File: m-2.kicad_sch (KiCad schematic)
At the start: 14 parts, among them Y2 Oscillator_SMD_32.768kHz_ECS_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

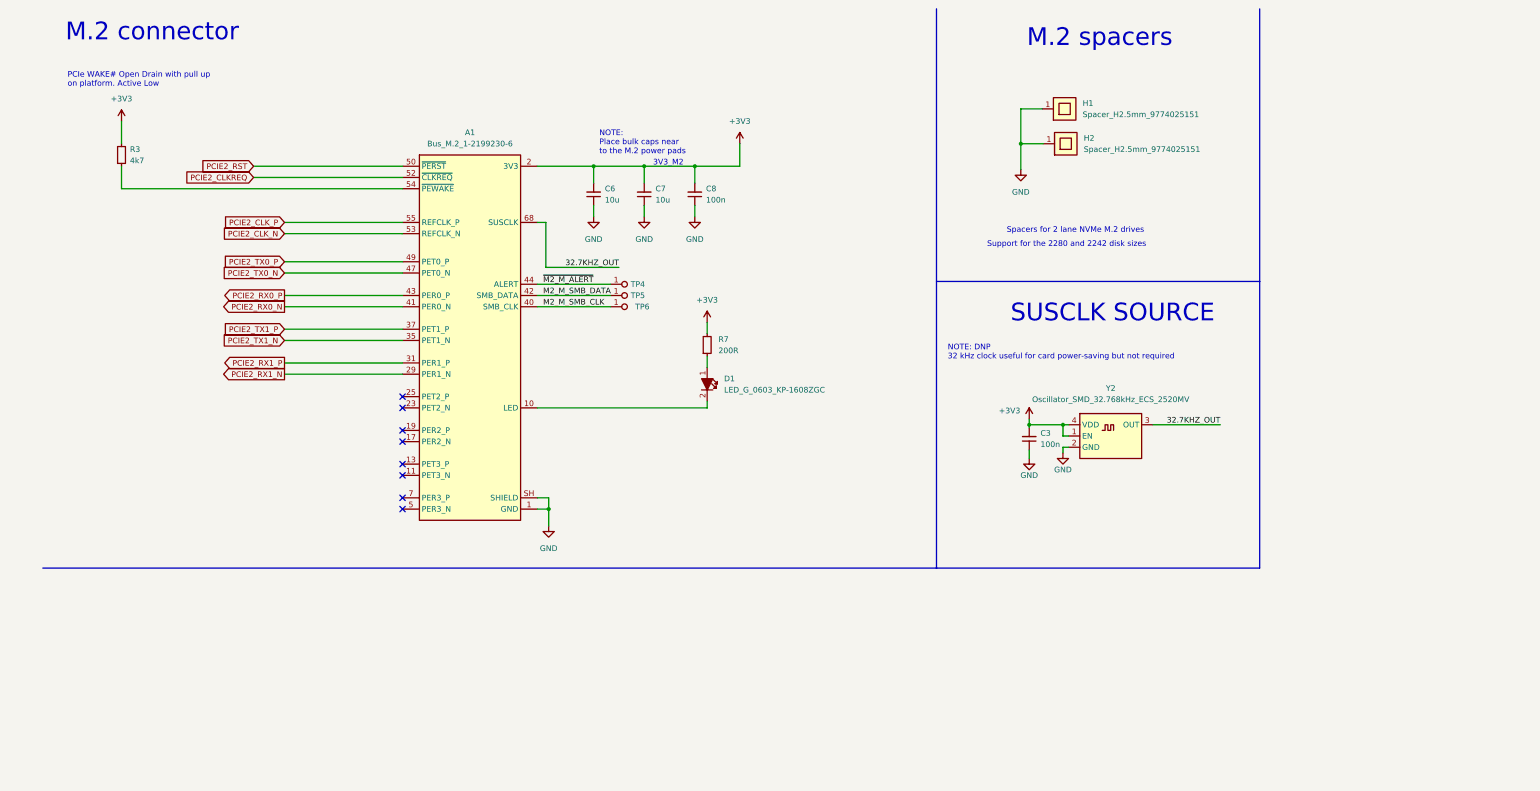
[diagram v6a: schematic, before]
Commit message: [#45990] Fix silk screen drcs
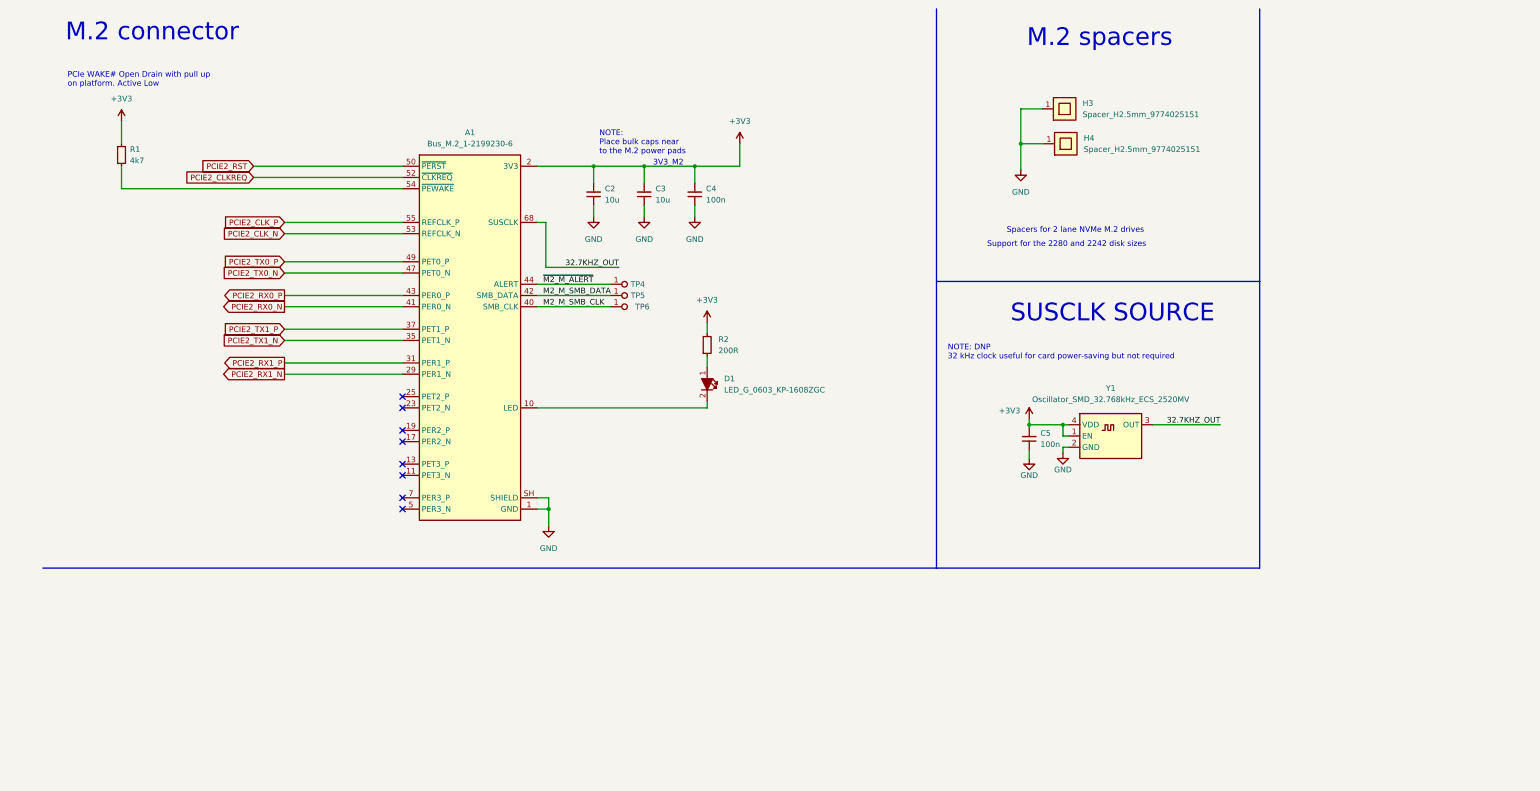
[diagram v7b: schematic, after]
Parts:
- renumbered C6 to C2, C7 to C3, C8 to C4, C3 to C5, H1 to H3, H2 to H4, R3 to R1, R7 to R2, Y2 to Y1
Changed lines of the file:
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@@
   (symbol (lib_id "antmicropower:GND") (at 136.525 59.055 0) (unit 1)
     (in_bom yes) (on_board yes) (fields_autoplaced)
-    (property "Reference" "#PWR011" (id 0) (at 136.525 65.405 0)
+    (property "Reference" "#PWR08" (id 0) (at 136.525 65.405 0)
       (effects (font (size 1.27 1.27)) hide)
     )
@@
   (symbol (lib_id "jetson-orin-baseboard:GND") (at 234.95 113.665 0) (mirror y) (unit 1)
     (in_bom yes) (on_board yes) (fields_autoplaced)
-    (property "Reference" "#PWR0106" (id 0) (at 234.95 120.015 0)
+    (property "Reference" "#PWR015" (id 0) (at 234.95 120.015 0)
       (effects (font (size 1.27 1.27)) hide)
     )
@@
   (symbol (lib_id "antmicropower:+3V3") (at 169.545 42.545 0) (unit 1)
     (in_bom yes) (on_board yes) (fields_autoplaced)
-    (property "Reference" "#PWR015" (id 0) (at 169.545 46.355 0)
+    (property "Reference" "#PWR012" (id 0) (at 169.545 46.355 0)
       (effects (font (size 1.27 1.27)) hide)
     )
@@
   (symbol (lib_id "antmicroMechanicalParts:Spacer_H2.5mm_9774025151") (at 237.871 34.671 0) (unit 1)
     (in_bom yes) (on_board yes) (fields_autoplaced)
-    (property "Reference" "H1" (id 0) (at 247.015 33.4009 0)
+    (property "Reference" "H3" (id 0) (at 247.015 33.4009 0)
       (effects (font (size 1.27 1.27) (thickness 0.15)) (justify left))
     )
@@
   (symbol (lib_id "antmicropower:GND") (at 159.385 59.055 0) (unit 1)
     (in_bom yes) (on_board yes) (fields_autoplaced)
-    (property "Reference" "#PWR014" (id 0) (at 159.385 65.405 0)
+    (property "Reference" "#PWR010" (id 0) (at 159.385 65.405 0)
       (effects (font (size 1.27 1.27)) hide)
     )
@@
   (symbol (lib_id "antmicroCapacitors0402:C_100n_0402") (at 234.95 111.76 90) (unit 1)
     (in_bom yes) (on_board yes) (fields_autoplaced)
-    (property "Reference" "C3" (id 0) (at 237.49 107.9435 90)
+    (property "Reference" "C5" (id 0) (at 237.49 107.9435 90)
       (effects (font (size 1.27 1.27) (thickness 0.15)) (justify right))
     )
@@
   (symbol (lib_id "antmicroResistors0402:R_200R_0402") (at 162.179 90.551 90) (unit 1)
     (in_bom yes) (on_board yes) (fields_autoplaced)
-    (property "Reference" "R7" (id 0) (at 164.719 86.7409 90)
+    (property "Reference" "R2" (id 0) (at 164.719 86.7409 90)
       (effects (font (size 1.27 1.27) (thickness 0.15)) (justify right))
     )
@@
   (symbol (lib_id "antmicroOscillators:Oscillator_SMD_32.768kHz_ECS_2520MV") (at 243.84 106.045 0) (unit 1)
     (in_bom yes) (on_board yes) (fields_autoplaced)
-    (property "Reference" "Y2" (id 0) (at 253.365 97.79 0)
+    (property "Reference" "Y1" (id 0) (at 253.365 97.79 0)
       (effects (font (size 1.27 1.27) (thickness 0.15)))
     )
@@
   (symbol (lib_id "antmicroCapacitors0402:C_10u_0402") (at 147.955 56.515 90) (unit 1)
     (in_bom yes) (on_board yes) (fields_autoplaced)
-    (property "Reference" "C7" (id 0) (at 150.495 52.6985 90)
+    (property "Reference" "C3" (id 0) (at 150.495 52.6985 90)
       (effects (font (size 1.27 1.27) (thickness 0.15)) (justify right))
     )
@@
   (symbol (lib_id "antmicropower:GND") (at 233.045 48.387 0) (unit 1)
     (in_bom yes) (on_board yes) (fields_autoplaced)
-    (property "Reference" "#PWR0101" (id 0) (at 233.045 54.737 0)
+    (property "Reference" "#PWR013" (id 0) (at 233.045 54.737 0)
       (effects (font (size 1.27 1.27)) hide)
     )
@@
   (symbol (lib_id "antmicropower:+3V3") (at 162.179 82.931 0) (unit 1)
     (in_bom yes) (on_board yes) (fields_autoplaced)
-    (property "Reference" "#PWR012" (id 0) (at 162.179 86.741 0)
+    (property "Reference" "#PWR011" (id 0) (at 162.179 86.741 0)
       (effects (font (size 1.27 1.27)) hide)
     )
@@
   (symbol (lib_id "antmicroResistors0402:R_4k7_0402") (at 29.845 47.625 90) (unit 1)
     (in_bom yes) (on_board yes) (fields_autoplaced)
-    (property "Reference" "R3" (id 0) (at 31.75 43.8149 90)
+    (property "Reference" "R1" (id 0) (at 31.75 43.8149 90)
       (effects (font (size 1.27 1.27) (thickness 0.15)) (justify right))
     )
@@
   (symbol (lib_id "antmicroMechanicalParts:Spacer_H2.5mm_9774025151") (at 238.125 42.545 0) (unit 1)
     (in_bom yes) (on_board yes) (fields_autoplaced)
-    (property "Reference" "H2" (id 0) (at 247.269 41.2749 0)
+    (property "Reference" "H4" (id 0) (at 247.269 41.2749 0)
       (effects (font (size 1.27 1.27) (thickness 0.15)) (justify left))
     )
@@
   (symbol (lib_id "antmicroCapacitors0603:C_100n_0603") (at 159.385 56.515 90) (unit 1)
     (in_bom yes) (on_board yes) (fields_autoplaced)
-    (property "Reference" "C8" (id 0) (at 161.925 52.6985 90)
+    (property "Reference" "C4" (id 0) (at 161.925 52.6985 90)
       (effects (font (size 1.27 1.27) (thickness 0.15)) (justify right))
     )
@@
   (symbol (lib_id "jetson-orin-baseboard:+3V3") (at 234.95 104.775 0) (unit 1)
     (in_bom yes) (on_board yes)
-    (property "Reference" "#PWR0107" (id 0) (at 234.95 108.585 0)
+    (property "Reference" "#PWR014" (id 0) (at 234.95 108.585 0)
       (effects (font (size 1.27 1.27)) hide)
     )
@@
   (symbol (lib_id "antmicroCapacitors0402:C_10u_0402") (at 136.525 56.515 90) (unit 1)
     (in_bom yes) (on_board yes) (fields_autoplaced)
-    (property "Reference" "C6" (id 0) (at 139.065 52.6985 90)
+    (property "Reference" "C2" (id 0) (at 139.065 52.6985 90)
       (effects (font (size 1.27 1.27) (thickness 0.15)) (justify right))
     )
@@
   (symbol (lib_id "jetson-orin-baseboard:GND") (at 242.57 112.395 0) (unit 1)
     (in_bom yes) (on_board yes) (fields_autoplaced)
-    (property "Reference" "#PWR0104" (id 0) (at 242.57 118.745 0)
+    (property "Reference" "#PWR016" (id 0) (at 242.57 118.745 0)
       (effects (font (size 1.27 1.27)) hide)
     )
@@
   (symbol (lib_id "antmicropower:+3V3") (at 29.845 37.465 0) (unit 1)
     (in_bom yes) (on_board yes) (fields_autoplaced)
-    (property "Reference" "#PWR09" (id 0) (at 29.845 41.275 0)
+    (property "Reference" "#PWR06" (id 0) (at 29.845 41.275 0)
       (effects (font (size 1.27 1.27)) hide)
     )
@@
   (symbol (lib_id "antmicropower:GND") (at 126.365 128.905 0) (unit 1)
     (in_bom yes) (on_board yes) (fields_autoplaced)
-    (property "Reference" "#PWR010" (id 0) (at 126.365 135.255 0)
+    (property "Reference" "#PWR07" (id 0) (at 126.365 135.255 0)
       (effects (font (size 1.27 1.27)) hide)
     )
@@
   (symbol (lib_id "antmicropower:GND") (at 147.955 59.055 0) (unit 1)
     (in_bom yes) (on_board yes) (fields_autoplaced)
-    (property "Reference" "#PWR013" (id 0) (at 147.955 65.405 0)
-      (effects (font (size 1.27 1.27)) hide)
-    )
+    (property "Reference" "#PWR09" (id 0) (at 147.955 65.405 0)
+      (effects (font (size 1.27 1.27)) hide)
+    )

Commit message: [#45990] Cosmetic changes for schematic, expand README
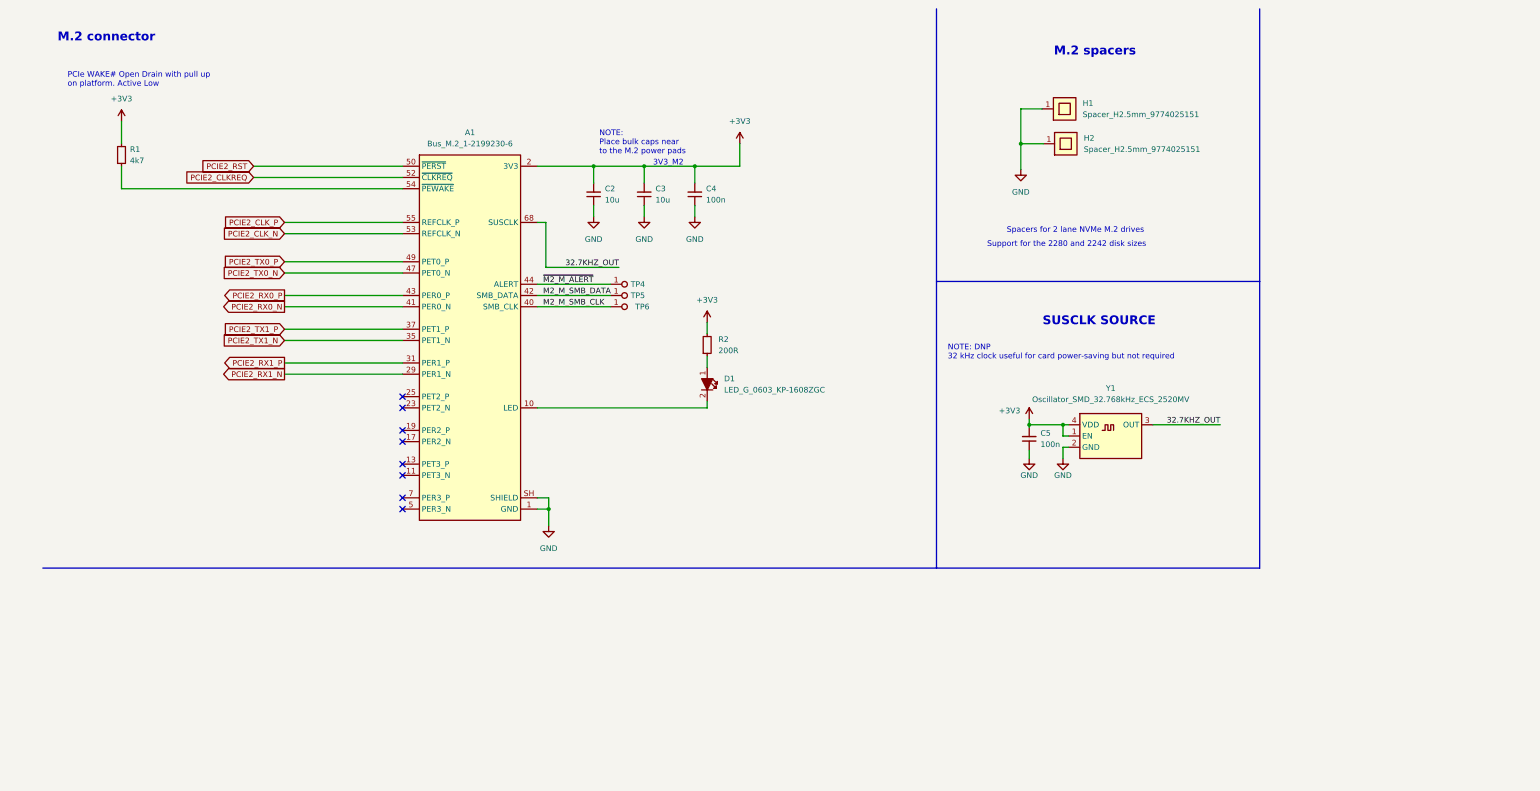
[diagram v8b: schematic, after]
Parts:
- renumbered H3 to H1, H4 to H2
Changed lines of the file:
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@@
     (stroke (width 0) (type default) (color 0 0 0 0))
   )
-  (wire (pts (xy 242.57 111.125) (xy 242.57 112.395))
+  (wire (pts (xy 242.57 111.125) (xy 242.57 113.665))
     (stroke (width 0) (type default) (color 0 0 0 0))
   )
@@
     (effects (font (size 1.27 1.27)) (justify left bottom))
   )
-  (text "M.2 spacers" (at 267.335 20.955 180)
-    (effects (font (size 4 4)) (justify right bottom))
-  )
-  (text "M.2 connector" (at 56.388 19.685 180)
-    (effects (font (size 4 4)) (justify right bottom))
+  (text "M.2 spacers" (at 259.08 22.86 180)
+    (effects (font (size 2 2) (thickness 0.4) bold) (justify right bottom))
+  )
+  (text "M.2 connector" (at 37.465 19.685 180)
+    (effects (font (size 2 2) (thickness 0.4) bold) (justify right bottom))
   )
   (text "Spacers for 2 lane NVMe M.2 drives" (at 229.87 62.865 0)
     (effects (font (size 1.27 1.27)) (justify left bottom))
   )
-  (text "SUSCLK SOURCE" (at 276.86 83.185 180)
-    (effects (font (size 4 4)) (justify right bottom))
+  (text "SUSCLK SOURCE" (at 263.525 83.82 180)
+    (effects (font (size 2 2) (thickness 0.4) bold) (justify right bottom))
   )
   (text "NOTE:\nPlace bulk caps near \nto the M.2 power pads" (at 137.795 45.085 0)
@@
   (symbol (lib_id "antmicropower:GND") (at 136.525 59.055 0) (unit 1)
     (in_bom yes) (on_board yes) (fields_autoplaced)
-    (property "Reference" "#PWR08" (id 0) (at 136.525 65.405 0)
+    (property "Reference" "#PWR07" (id 0) (at 136.525 65.405 0)
       (effects (font (size 1.27 1.27)) hide)
     )
@@
   (symbol (lib_id "jetson-orin-baseboard:GND") (at 234.95 113.665 0) (mirror y) (unit 1)
     (in_bom yes) (on_board yes) (fields_autoplaced)
-    (property "Reference" "#PWR015" (id 0) (at 234.95 120.015 0)
+    (property "Reference" "#PWR014" (id 0) (at 234.95 120.015 0)
       (effects (font (size 1.27 1.27)) hide)
     )
@@
   (symbol (lib_id "antmicropower:+3V3") (at 169.545 42.545 0) (unit 1)
     (in_bom yes) (on_board yes) (fields_autoplaced)
-    (property "Reference" "#PWR012" (id 0) (at 169.545 46.355 0)
+    (property "Reference" "#PWR011" (id 0) (at 169.545 46.355 0)
       (effects (font (size 1.27 1.27)) hide)
     )
@@
   (symbol (lib_id "antmicroMechanicalParts:Spacer_H2.5mm_9774025151") (at 237.871 34.671 0) (unit 1)
     (in_bom yes) (on_board yes) (fields_autoplaced)
-    (property "Reference" "H3" (id 0) (at 247.015 33.4009 0)
+    (property "Reference" "H1" (id 0) (at 247.015 33.4009 0)
       (effects (font (size 1.27 1.27) (thickness 0.15)) (justify left))
     )
@@
   (symbol (lib_id "antmicropower:GND") (at 159.385 59.055 0) (unit 1)
     (in_bom yes) (on_board yes) (fields_autoplaced)
-    (property "Reference" "#PWR010" (id 0) (at 159.385 65.405 0)
+    (property "Reference" "#PWR09" (id 0) (at 159.385 65.405 0)
       (effects (font (size 1.27 1.27)) hide)
     )
@@
   (symbol (lib_id "antmicropower:GND") (at 233.045 48.387 0) (unit 1)
     (in_bom yes) (on_board yes) (fields_autoplaced)
-    (property "Reference" "#PWR013" (id 0) (at 233.045 54.737 0)
+    (property "Reference" "#PWR012" (id 0) (at 233.045 54.737 0)
       (effects (font (size 1.27 1.27)) hide)
     )
@@
   (symbol (lib_id "antmicropower:+3V3") (at 162.179 82.931 0) (unit 1)
     (in_bom yes) (on_board yes) (fields_autoplaced)
-    (property "Reference" "#PWR011" (id 0) (at 162.179 86.741 0)
+    (property "Reference" "#PWR010" (id 0) (at 162.179 86.741 0)
       (effects (font (size 1.27 1.27)) hide)
     )
@@
   (symbol (lib_id "antmicroMechanicalParts:Spacer_H2.5mm_9774025151") (at 238.125 42.545 0) (unit 1)
     (in_bom yes) (on_board yes) (fields_autoplaced)
-    (property "Reference" "H4" (id 0) (at 247.269 41.2749 0)
+    (property "Reference" "H2" (id 0) (at 247.269 41.2749 0)
       (effects (font (size 1.27 1.27) (thickness 0.15)) (justify left))
     )
@@
   (symbol (lib_id "jetson-orin-baseboard:+3V3") (at 234.95 104.775 0) (unit 1)
     (in_bom yes) (on_board yes)
-    (property "Reference" "#PWR014" (id 0) (at 234.95 108.585 0)
+    (property "Reference" "#PWR013" (id 0) (at 234.95 108.585 0)
       (effects (font (size 1.27 1.27)) hide)
     )
@@
     (pin "2")
   )
-  (symbol (lib_id "jetson-orin-baseboard:GND") (at 242.57 112.395 0) (unit 1)
+  (symbol (lib_id "jetson-orin-baseboard:GND") (at 242.57 113.665 0) (unit 1)
     (in_bom yes) (on_board yes) (fields_autoplaced)
-    (property "Reference" "#PWR016" (id 0) (at 242.57 118.745 0)
-      (effects (font (size 1.27 1.27)) hide)
-    )
-    (property "Value" "GND" (id 1) (at 242.57 116.205 0))
-    (property "Footprint" "" (id 2) (at 242.57 112.395 0)
-      (effects (font (size 1.27 1.27)) hide)
-    )
-    (property "Datasheet" "" (id 3) (at 242.57 112.395 0)
+    (property "Reference" "#PWR015" (id 0) (at 242.57 120.015 0)
+      (effects (font (size 1.27 1.27)) hide)
+    )
+    (property "Value" "GND" (id 1) (at 242.57 117.475 0))
+    (property "Footprint" "" (id 2) (at 242.57 113.665 0)
+      (effects (font (size 1.27 1.27)) hide)
+    )
+    (property "Datasheet" "" (id 3) (at 242.57 113.665 0)
       (effects (font (size 1.27 1.27)) hide)
     )
@@
   (symbol (lib_id "antmicropower:+3V3") (at 29.845 37.465 0) (unit 1)
     (in_bom yes) (on_board yes) (fields_autoplaced)
-    (property "Reference" "#PWR06" (id 0) (at 29.845 41.275 0)
+    (property "Reference" "#PWR05" (id 0) (at 29.845 41.275 0)
       (effects (font (size 1.27 1.27)) hide)
     )
@@
   (symbol (lib_id "antmicropower:GND") (at 126.365 128.905 0) (unit 1)
     (in_bom yes) (on_board yes) (fields_autoplaced)
-    (property "Reference" "#PWR07" (id 0) (at 126.365 135.255 0)
+    (property "Reference" "#PWR06" (id 0) (at 126.365 135.255 0)
       (effects (font (size 1.27 1.27)) hide)
     )
@@
   (symbol (lib_id "antmicropower:GND") (at 147.955 59.055 0) (unit 1)
     (in_bom yes) (on_board yes) (fields_autoplaced)
-    (property "Reference" "#PWR09" (id 0) (at 147.955 65.405 0)
-      (effects (font (size 1.27 1.27)) hide)
-    )
+    (property "Reference" "#PWR08" (id 0) (at 147.955 65.405 0)
+      (effects (font (size 1.27 1.27)) hide)
+    )
